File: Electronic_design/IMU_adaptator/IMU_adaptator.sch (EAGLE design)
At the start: 5 parts, among them J1 CLM-110-02-XX-D

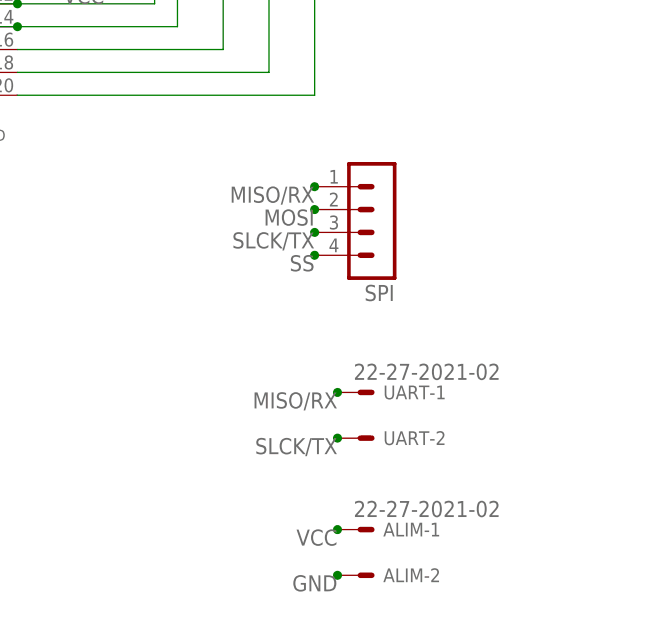
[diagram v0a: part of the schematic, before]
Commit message: reroutage carte IMU et STEPPER
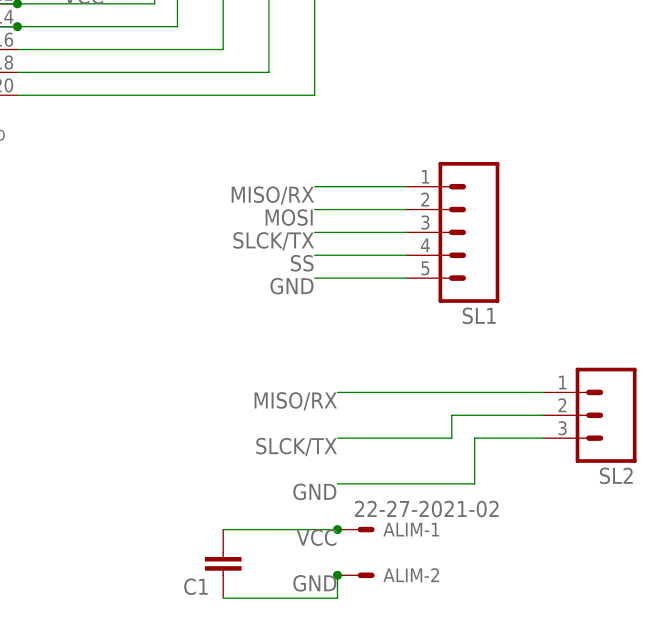
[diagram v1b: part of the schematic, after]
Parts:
- removed SPI: (no value), con-lstb:MA04-1
- removed UART: 22-27-2021-02, con-molex:22-27-2021-02
- added C1: (no value), eagle-ltspice:C
- added SL1: (no value), con-amp-quick:MA05
- added SL2: (no value), con-amp-quick:MA03
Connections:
- net GND: now also C1.1, SL1.5, SL2.3
- net MISO/RX: now also SL1.1, SL2.1; no longer SPI.1, UART-1.S
- net MOSI: now also SL1.2; no longer SPI.2
- net SLCK/TX: now also SL1.3, SL2.2; no longer SPI.3, UART-2.S
- net SS: now also SL1.4; no longer SPI.4
- net VCC: now also C1.2
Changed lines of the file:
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@@
 <?xml version="1.0" encoding="utf-8"?>
 <!DOCTYPE eagle SYSTEM "eagle.dtd">
-<eagle version="8.4.1">
+<eagle version="6.5.0">
 <drawing>
 <settings>
@@
 <layer number="97" name="Info" color="7" fill="1" visible="yes" active="yes"/>
 <layer number="98" name="Guide" color="6" fill="1" visible="yes" active="yes"/>
+<layer number="99" name="SpiceOrder" color="5" fill="1" visible="yes" active="yes"/>
 </layers>
 <schematic xreflabel="%F%N/%S.%C%R" xrefpart="/%S.%C%R">
@@
 <parts>
 <part name="J1" library="CLM-110-02-XX-D" deviceset="CLM-110-02-XX-D" device=""/>
-<part name="SV1" library="con-lsta" library_urn="urn:adsk.eagle:library:161" deviceset="FE10-2" device="" package3d_urn="urn:adsk.eagle:package:8177/1"/>
-<part name="SPI" library="con-lstb" library_urn="urn:adsk.eagle:library:162" deviceset="MA04-1" device="" package3d_urn="urn:adsk.eagle:package:8337/1"/>
-<part name="UART" library="con-molex" library_urn="urn:adsk.eagle:library:165" deviceset="22-?-02" device="27-2021"/>
-<part name="ALIM" library="con-molex" library_urn="urn:adsk.eagle:library:165" deviceset="22-?-02" device="27-2021"/>
+<part name="SV1" library="con-lsta" deviceset="FE10-2" device=""/>
+<part name="ALIM" library="con-molex" deviceset="22-?-02" device="27-2021"/>
+<part name="C1" library="eagle-ltspice" deviceset="C" device=""/>
+<part name="SL1" library="con-amp-quick" deviceset="MA05" device=""/>
+<part name="SL2" library="con-amp-quick" deviceset="MA03" device=""/>
 </parts>
 <sheets>
@@
 <instance part="J1" gate="G$1" x="22.86" y="38.1"/>
 <instance part="SV1" gate="G$1" x="33.02" y="55.88"/>
-<instance part="SPI" gate="1" x="83.82" y="0" rot="R180"/>
-<instance part="UART" gate="-1" x="81.28" y="-17.78"/>
-<instance part="UART" gate="-2" x="81.28" y="-22.86"/>
 <instance part="ALIM" gate="-1" x="81.28" y="-33.02"/>
 <instance part="ALIM" gate="-2" x="81.28" y="-38.1"/>
+<instance part="C1" gate="G$1" x="66.04" y="-38.1" rot="R180"/>
+<instance part="SL1" gate="G$1" x="93.98" y="0" rot="R180"/>
+<instance part="SL2" gate="G$1" x="109.22" y="-20.32" rot="R180"/>
 </instances>
 <busses>
@@
 <junction x="78.74" y="-38.1"/>
 <label x="78.74" y="-38.1" size="1.778" layer="95" rot="R180"/>
+<pinref part="C1" gate="G$1" pin="1"/>
+<wire x1="66.04" y1="-40.64" x2="78.74" y2="-40.64" width="0.1524" layer="91"/>
+<wire x1="78.74" y1="-40.64" x2="78.74" y2="-38.1" width="0.1524" layer="91"/>
+</segment>
+<segment>
+<pinref part="SL1" gate="G$1" pin="5"/>
+<wire x1="86.36" y1="-5.08" x2="76.2" y2="-5.08" width="0.1524" layer="91"/>
+<label x="76.2" y="-5.08" size="1.778" layer="95" rot="R180"/>
+</segment>
+<segment>
+<pinref part="SL2" gate="G$1" pin="3"/>
+<wire x1="101.6" y1="-22.86" x2="93.98" y2="-22.86" width="0.1524" layer="91"/>
+<wire x1="93.98" y1="-22.86" x2="93.98" y2="-27.94" width="0.1524" layer="91"/>
+<wire x1="93.98" y1="-27.94" x2="78.74" y2="-27.94" width="0.1524" layer="91"/>
+<label x="78.74" y="-27.94" size="1.778" layer="95" rot="R180"/>
 </segment>
 </net>
@@
 <junction x="78.74" y="-33.02"/>
 <label x="78.74" y="-33.02" size="1.778" layer="95" rot="R180"/>
+<pinref part="C1" gate="G$1" pin="2"/>
+<wire x1="66.04" y1="-33.02" x2="78.74" y2="-33.02" width="0.1524" layer="91"/>
 </segment>
 <segment>
@@
 <net name="SLCK/TX" class="0">
 <segment>
-<pinref part="UART" gate="-2" pin="S"/>
-<junction x="78.74" y="-22.86"/>
 <label x="78.74" y="-22.86" size="1.778" layer="95" rot="R180"/>
-</segment>
-<segment>
-<pinref part="SPI" gate="1" pin="3"/>
-<junction x="76.2" y="0"/>
+<wire x1="78.74" y1="-22.86" x2="91.44" y2="-22.86" width="0.1524" layer="91"/>
+<wire x1="91.44" y1="-22.86" x2="91.44" y2="-20.32" width="0.1524" layer="91"/>
+<pinref part="SL2" gate="G$1" pin="2"/>
+<wire x1="91.44" y1="-20.32" x2="101.6" y2="-20.32" width="0.1524" layer="91"/>
+</segment>
+<segment>
 <label x="76.2" y="0" size="1.778" layer="95" rot="R180"/>
+<pinref part="SL1" gate="G$1" pin="3"/>
+<wire x1="76.2" y1="0" x2="86.36" y2="0" width="0.1524" layer="91"/>
 </segment>
 <segment>
@@
 <net name="MISO/RX" class="0">
 <segment>
-<pinref part="UART" gate="-1" pin="S"/>
-<junction x="78.74" y="-17.78"/>
 <label x="78.74" y="-17.78" size="1.778" layer="95" rot="R180"/>
-</segment>
-<segment>
-<pinref part="SPI" gate="1" pin="1"/>
-<junction x="76.2" y="5.08"/>
+<pinref part="SL2" gate="G$1" pin="1"/>
+<wire x1="78.74" y1="-17.78" x2="101.6" y2="-17.78" width="0.1524" layer="91"/>
+</segment>
+<segment>
 <label x="76.2" y="5.08" size="1.778" layer="95" rot="R180"/>
+<pinref part="SL1" gate="G$1" pin="1"/>
+<wire x1="76.2" y1="5.08" x2="86.36" y2="5.08" width="0.1524" layer="91"/>
 </segment>
 <segment>
@@
 <net name="MOSI" class="0">
 <segment>
-<pinref part="SPI" gate="1" pin="2"/>
-<junction x="76.2" y="2.54"/>
 <label x="76.2" y="2.54" size="1.778" layer="95" rot="R180"/>
+<pinref part="SL1" gate="G$1" pin="2"/>
+<wire x1="76.2" y1="2.54" x2="86.36" y2="2.54" width="0.1524" layer="91"/>
 </segment>
 <segment>
@@
 <net name="SS" class="0">
 <segment>
-<pinref part="SPI" gate="1" pin="4"/>
-<junction x="76.2" y="-2.54"/>
 <label x="76.2" y="-2.54" size="1.778" layer="95" rot="R180"/>
+<pinref part="SL1" gate="G$1" pin="4"/>
+<wire x1="76.2" y1="-2.54" x2="86.36" y2="-2.54" width="0.1524" layer="91"/>
 </segment>
 <segment>
@@
 </schematic>
 </drawing>
-<compatibility>
-<note version="8.2" severity="warning">
-Since Version 8.2, EAGLE supports online libraries. The ids
-of those online libraries will not be understood (or retained)
-with this version.
-</note>
-<note version="8.3" severity="warning">
-Since Version 8.3, EAGLE supports URNs for individual library
-assets (packages, symbols, and devices). The URNs of those assets
-will not be understood (or retained) with this version.
-</note>
-<note version="8.3" severity="warning">
-Since Version 8.3, EAGLE supports the association of 3D packages
-with devices in libraries, schematics, and board files. Those 3D
-packages will not be understood (or retained) with this version.
-</note>
-</compatibility>
 </eagle>

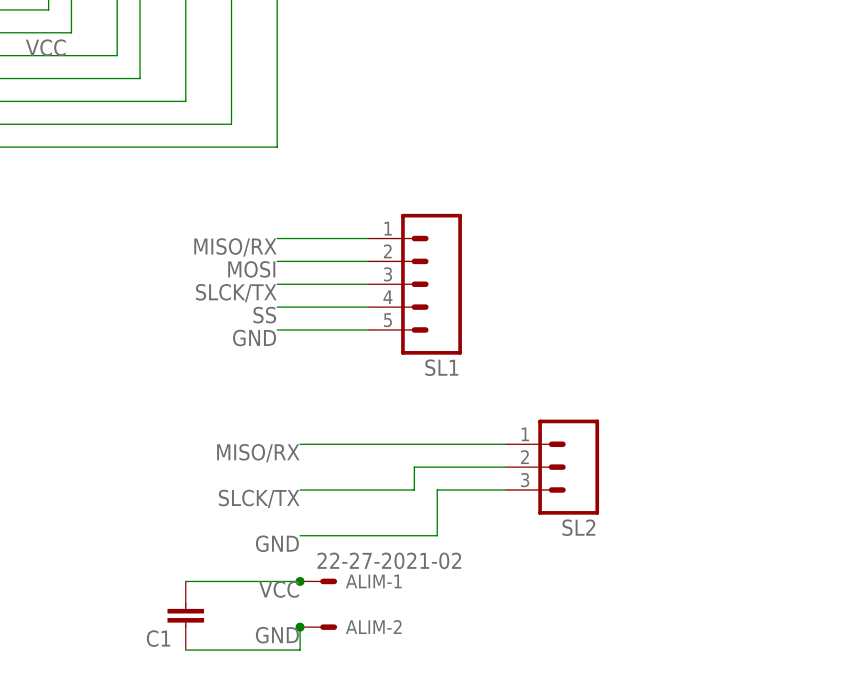
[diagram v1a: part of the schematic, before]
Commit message: ajout alim aux connect SPI et UART
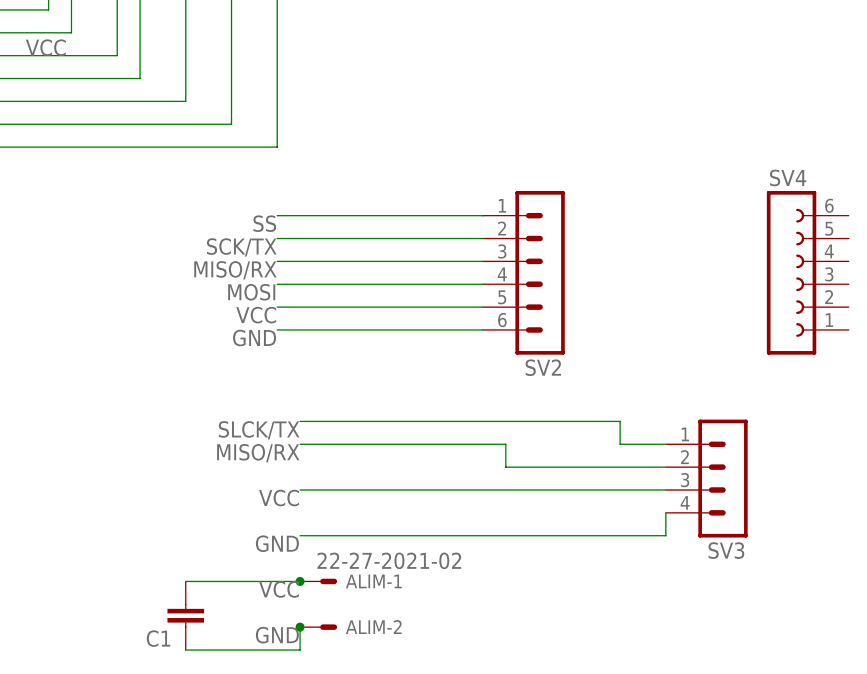
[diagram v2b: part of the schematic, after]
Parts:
- removed SL1: (no value), con-amp-quick:MA05
- removed SL2: (no value), con-amp-quick:MA03
- added SV2: (no value), con-lstb:MA06-1
- added SV3: (no value), con-lstb:MA04-1
- added SV4: (no value), con-lsta:FE06-1
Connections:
- new net SCK/TX: SV2.2
- net GND: now also SV2.6, SV3.4; no longer SL1.5, SL2.3
- net MISO/RX: now also SV2.3, SV3.2; no longer SL1.1, SL2.1
- net MOSI: now also SV2.4; no longer SL1.2
- net SLCK/TX: now also SV3.1; no longer SL1.3, SL2.2
- net SS: now also SV2.1; no longer SL1.4
- net VCC: now also SV2.5, SV3.3
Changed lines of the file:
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@@
 <?xml version="1.0" encoding="utf-8"?>
 <!DOCTYPE eagle SYSTEM "eagle.dtd">
-<eagle version="6.5.0">
+<eagle version="8.4.1">
 <drawing>
 <settings>
 <setting alwaysvectorfont="no"/>
+<setting keepoldvectorfont="yes"/>
 <setting verticaltext="up"/>
 </settings>
@@
 <part name="ALIM" library="con-molex" deviceset="22-?-02" device="27-2021"/>
 <part name="C1" library="eagle-ltspice" deviceset="C" device=""/>
-<part name="SL1" library="con-amp-quick" deviceset="MA05" device=""/>
-<part name="SL2" library="con-amp-quick" deviceset="MA03" device=""/>
+<part name="SV2" library="con-lstb" library_urn="urn:adsk.eagle:library:162" deviceset="MA06-1" device="" package3d_urn="urn:adsk.eagle:package:8340/1"/>
+<part name="SV3" library="con-lstb" library_urn="urn:adsk.eagle:library:162" deviceset="MA04-1" device="" package3d_urn="urn:adsk.eagle:package:8337/1"/>
+<part name="SV4" library="con-lsta" library_urn="urn:adsk.eagle:library:161" deviceset="FE06-1" device="" package3d_urn="urn:adsk.eagle:package:8191/1"/>
 </parts>
 <sheets>
@@
 <instance part="ALIM" gate="-2" x="81.28" y="-38.1"/>
 <instance part="C1" gate="G$1" x="66.04" y="-38.1" rot="R180"/>
-<instance part="SL1" gate="G$1" x="93.98" y="0" rot="R180"/>
-<instance part="SL2" gate="G$1" x="109.22" y="-20.32" rot="R180"/>
+<instance part="SV2" gate="1" x="106.68" y="0" rot="R180"/>
+<instance part="SV3" gate="1" x="127" y="-22.86" rot="R180"/>
+<instance part="SV4" gate="G$1" x="132.08" y="0"/>
 </instances>
 <busses>
@@
 </segment>
 <segment>
-<pinref part="SL1" gate="G$1" pin="5"/>
-<wire x1="86.36" y1="-5.08" x2="76.2" y2="-5.08" width="0.1524" layer="91"/>
 <label x="76.2" y="-5.08" size="1.778" layer="95" rot="R180"/>
-</segment>
-<segment>
-<pinref part="SL2" gate="G$1" pin="3"/>
-<wire x1="101.6" y1="-22.86" x2="93.98" y2="-22.86" width="0.1524" layer="91"/>
-<wire x1="93.98" y1="-22.86" x2="93.98" y2="-27.94" width="0.1524" layer="91"/>
-<wire x1="93.98" y1="-27.94" x2="78.74" y2="-27.94" width="0.1524" layer="91"/>
+<pinref part="SV2" gate="1" pin="6"/>
+<wire x1="76.2" y1="-5.08" x2="99.06" y2="-5.08" width="0.1524" layer="91"/>
+</segment>
+<segment>
 <label x="78.74" y="-27.94" size="1.778" layer="95" rot="R180"/>
+<pinref part="SV3" gate="1" pin="4"/>
+<wire x1="119.38" y1="-25.4" x2="119.38" y2="-27.94" width="0.1524" layer="91"/>
+<wire x1="119.38" y1="-27.94" x2="78.74" y2="-27.94" width="0.1524" layer="91"/>
 </segment>
 </net>
@@
 <label x="48.26" y="25.4" size="1.778" layer="95"/>
 </segment>
+<segment>
+<pinref part="SV2" gate="1" pin="5"/>
+<wire x1="99.06" y1="-2.54" x2="76.2" y2="-2.54" width="0.1524" layer="91"/>
+<label x="76.2" y="-2.54" size="1.778" layer="95" rot="R180"/>
+</segment>
+<segment>
+<pinref part="SV3" gate="1" pin="3"/>
+<wire x1="119.38" y1="-22.86" x2="78.74" y2="-22.86" width="0.1524" layer="91"/>
+<label x="78.74" y="-22.86" size="1.778" layer="95" rot="R180"/>
+</segment>
 </net>
 <net name="SLCK/TX" class="0">
 <segment>
-<label x="78.74" y="-22.86" size="1.778" layer="95" rot="R180"/>
-<wire x1="78.74" y1="-22.86" x2="91.44" y2="-22.86" width="0.1524" layer="91"/>
-<wire x1="91.44" y1="-22.86" x2="91.44" y2="-20.32" width="0.1524" layer="91"/>
-<pinref part="SL2" gate="G$1" pin="2"/>
-<wire x1="91.44" y1="-20.32" x2="101.6" y2="-20.32" width="0.1524" layer="91"/>
-</segment>
-<segment>
-<label x="76.2" y="0" size="1.778" layer="95" rot="R180"/>
-<pinref part="SL1" gate="G$1" pin="3"/>
-<wire x1="76.2" y1="0" x2="86.36" y2="0" width="0.1524" layer="91"/>
+<label x="78.74" y="-15.24" size="1.778" layer="95" rot="R180"/>
+<wire x1="78.74" y1="-15.24" x2="114.3" y2="-15.24" width="0.1524" layer="91"/>
+<pinref part="SV3" gate="1" pin="1"/>
+<wire x1="114.3" y1="-15.24" x2="114.3" y2="-17.78" width="0.1524" layer="91"/>
+<wire x1="114.3" y1="-17.78" x2="119.38" y2="-17.78" width="0.1524" layer="91"/>
 </segment>
 <segment>
@@
 <segment>
 <label x="78.74" y="-17.78" size="1.778" layer="95" rot="R180"/>
-<pinref part="SL2" gate="G$1" pin="1"/>
 <wire x1="78.74" y1="-17.78" x2="101.6" y2="-17.78" width="0.1524" layer="91"/>
-</segment>
-<segment>
-<label x="76.2" y="5.08" size="1.778" layer="95" rot="R180"/>
-<pinref part="SL1" gate="G$1" pin="1"/>
-<wire x1="76.2" y1="5.08" x2="86.36" y2="5.08" width="0.1524" layer="91"/>
+<pinref part="SV3" gate="1" pin="2"/>
+<wire x1="101.6" y1="-17.78" x2="101.6" y2="-20.32" width="0.1524" layer="91"/>
+<wire x1="101.6" y1="-20.32" x2="119.38" y2="-20.32" width="0.1524" layer="91"/>
 </segment>
 <segment>
@@
 <label x="45.72" y="35.56" size="1.778" layer="95" rot="R90"/>
 </segment>
+<segment>
+<pinref part="SV2" gate="1" pin="3"/>
+<wire x1="76.2" y1="2.54" x2="99.06" y2="2.54" width="0.1524" layer="91"/>
+<label x="76.2" y="2.54" size="1.778" layer="95" rot="R180"/>
+</segment>
 </net>
 <net name="MOSI" class="0">
-<segment>
-<label x="76.2" y="2.54" size="1.778" layer="95" rot="R180"/>
-<pinref part="SL1" gate="G$1" pin="2"/>
-<wire x1="76.2" y1="2.54" x2="86.36" y2="2.54" width="0.1524" layer="91"/>
-</segment>
 <segment>
 <pinref part="SV1" gate="G$1" pin="5"/>
@@
 <label x="15.24" y="33.02" size="1.778" layer="95"/>
 </segment>
+<segment>
+<pinref part="SV2" gate="1" pin="4"/>
+<wire x1="76.2" y1="0" x2="99.06" y2="0" width="0.1524" layer="91"/>
+<label x="76.2" y="0" size="1.778" layer="95" rot="R180"/>
+</segment>
 </net>
 <net name="SS" class="0">
-<segment>
-<label x="76.2" y="-2.54" size="1.778" layer="95" rot="R180"/>
-<pinref part="SL1" gate="G$1" pin="4"/>
-<wire x1="76.2" y1="-2.54" x2="86.36" y2="-2.54" width="0.1524" layer="91"/>
-</segment>
 <segment>
 <pinref part="SV1" gate="G$1" pin="6"/>
@@
 <label x="45.72" y="33.02" size="1.778" layer="95"/>
 </segment>
+<segment>
+<pinref part="SV2" gate="1" pin="1"/>
+<wire x1="76.2" y1="7.62" x2="99.06" y2="7.62" width="0.1524" layer="91"/>
+<label x="76.2" y="7.62" size="1.778" layer="95" rot="R180"/>
+</segment>
+</net>
+<net name="SCK/TX" class="0">
+<segment>
+<pinref part="SV2" gate="1" pin="2"/>
+<wire x1="99.06" y1="5.08" x2="76.2" y2="5.08" width="0.1524" layer="91"/>
+<label x="76.2" y="5.08" size="1.778" layer="95" rot="R180"/>
+</segment>
 </net>
 </nets>
@@
 </schematic>
 </drawing>
+<compatibility>
+<note version="8.2" severity="warning">
+Since Version 8.2, EAGLE supports online libraries. The ids
+of those online libraries will not be understood (or retained)
+with this version.
+</note>
+<note version="8.3" severity="warning">
+Since Version 8.3, EAGLE supports URNs for individual library
+assets (packages, symbols, and devices). The URNs of those assets
+will not be understood (or retained) with this version.
+</note>
+<note version="8.3" severity="warning">
+Since Version 8.3, EAGLE supports the association of 3D packages
+with devices in libraries, schematics, and board files. Those 3D
+packages will not be understood (or retained) with this version.
+</note>
+</compatibility>
 </eagle>

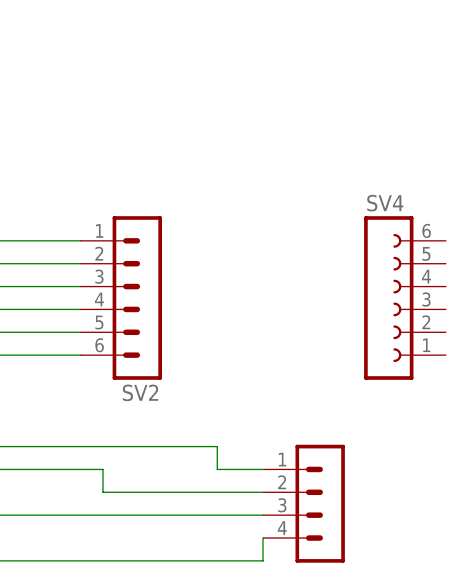
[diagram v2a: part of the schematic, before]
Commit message: suppression connecteur inutile
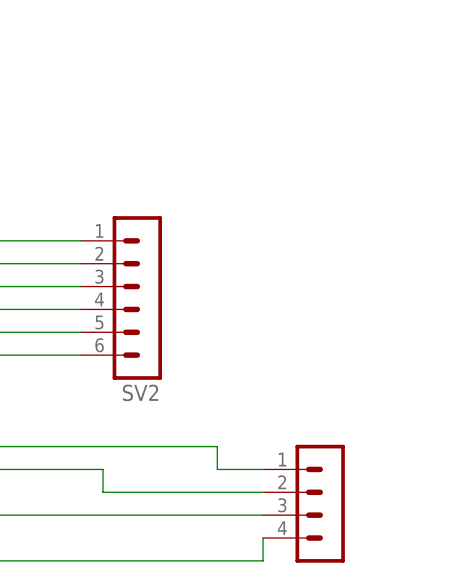
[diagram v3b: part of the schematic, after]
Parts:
- removed SV4: (no value), con-lsta:FE06-1
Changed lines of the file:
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@@
 <part name="SV2" library="con-lstb" library_urn="urn:adsk.eagle:library:162" deviceset="MA06-1" device="" package3d_urn="urn:adsk.eagle:package:8340/1"/>
 <part name="SV3" library="con-lstb" library_urn="urn:adsk.eagle:library:162" deviceset="MA04-1" device="" package3d_urn="urn:adsk.eagle:package:8337/1"/>
-<part name="SV4" library="con-lsta" library_urn="urn:adsk.eagle:library:161" deviceset="FE06-1" device="" package3d_urn="urn:adsk.eagle:package:8191/1"/>
 </parts>
 <sheets>
@@
 <instance part="SV2" gate="1" x="106.68" y="0" rot="R180"/>
 <instance part="SV3" gate="1" x="127" y="-22.86" rot="R180"/>
-<instance part="SV4" gate="G$1" x="132.08" y="0"/>
 </instances>
 <busses>

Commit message: ajout LED
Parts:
- added R1: (no value), rcl:R-EU_0204/5
- added VCC: (no value), eagle-ltspice:LED_ELD260
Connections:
- new net N$7: R1.2, VCC.A
- net GND: now also VCC.C
- net VCC: now also R1.1
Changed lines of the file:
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@@
 <part name="SV2" library="con-lstb" library_urn="urn:adsk.eagle:library:162" deviceset="MA06-1" device="" package3d_urn="urn:adsk.eagle:package:8340/1"/>
 <part name="SV3" library="con-lstb" library_urn="urn:adsk.eagle:library:162" deviceset="MA04-1" device="" package3d_urn="urn:adsk.eagle:package:8337/1"/>
+<part name="R1" library="rcl" library_urn="urn:adsk.eagle:library:334" deviceset="R-EU_" device="0204/5" package3d_urn="urn:adsk.eagle:package:23488/1"/>
+<part name="VCC" library="eagle-ltspice" library_urn="urn:adsk.eagle:library:217" deviceset="LED_E" device="LD260" package3d_urn="urn:adsk.eagle:package:13313/1"/>
 </parts>
 <sheets>
@@
 <instance part="SV2" gate="1" x="106.68" y="0" rot="R180"/>
 <instance part="SV3" gate="1" x="127" y="-22.86" rot="R180"/>
+<instance part="R1" gate="G$1" x="48.26" y="-38.1" rot="R270"/>
+<instance part="VCC" gate="G$1" x="48.26" y="-45.72"/>
 </instances>
 <busses>
@@
 <wire x1="66.04" y1="-40.64" x2="78.74" y2="-40.64" width="0.1524" layer="91"/>
 <wire x1="78.74" y1="-40.64" x2="78.74" y2="-38.1" width="0.1524" layer="91"/>
+<wire x1="66.04" y1="-40.64" x2="66.04" y2="-50.8" width="0.1524" layer="91"/>
+<junction x="66.04" y="-40.64"/>
+<pinref part="VCC" gate="G$1" pin="C"/>
+<wire x1="66.04" y1="-50.8" x2="48.26" y2="-50.8" width="0.1524" layer="91"/>
 </segment>
 <segment>
@@
 <pinref part="C1" gate="G$1" pin="2"/>
 <wire x1="66.04" y1="-33.02" x2="78.74" y2="-33.02" width="0.1524" layer="91"/>
+<pinref part="R1" gate="G$1" pin="1"/>
+<wire x1="66.04" y1="-33.02" x2="48.26" y2="-33.02" width="0.1524" layer="91"/>
+<junction x="66.04" y="-33.02"/>
 </segment>
 <segment>
@@
 </segment>
 </net>
+<net name="N$7" class="0">
+<segment>
+<pinref part="R1" gate="G$1" pin="2"/>
+<pinref part="VCC" gate="G$1" pin="A"/>
+</segment>
+</net>

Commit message: nouveau routage
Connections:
- net N$1 renamed 1
- net N$2 renamed 2
- net N$20 renamed 20
- net SCK/TX: now also J1.3, SV1.3
- net SLCK/TX: no longer J1.3, SV1.3
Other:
- moved on the sheet: SV1
